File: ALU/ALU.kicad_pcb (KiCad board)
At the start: 4 copper layers, 100 x 100 mm, 78 parts, among them IC1 SN74AHCT16245DGGR, J1 Conn_01x06_Pin, J2 Conn_02x15_Odd_Even, J3 Conn_02x15_Odd_Even, J4 Conn_02x15_Odd_Even, J5 Conn_01x01_Pin, J6 Conn_01x01_Pin, J7 Conn_01x01_Pin, J8 Conn_01x01_Pin, J9 Conn_01x02, U1 74AHC1G08, U10 74HCT21, U11 74AHC1G32DBVR, U12 74AHCT1G02DBVR, U13 74AHCT1G08DBVR, U14 74AHCT1G08DBVR, U15 74AHC1G32DBVR, U16 74AHC1G32DBVR, U17 74AHC1G08, U18 SN74AHCT16374DGGR, U19 74AHCT1G08DBVR, U2 SN74AHCT16374DGGR, U20 74AHCT1G02DBVR, U21 74AHCT1G02DBVR, U3 74AHC1G04DBVR, U4 74LS181, U5 74LS181, U6 74AHCT1G08DBVR, U7 74HCT11, U8 74LS181, U9 74LS181

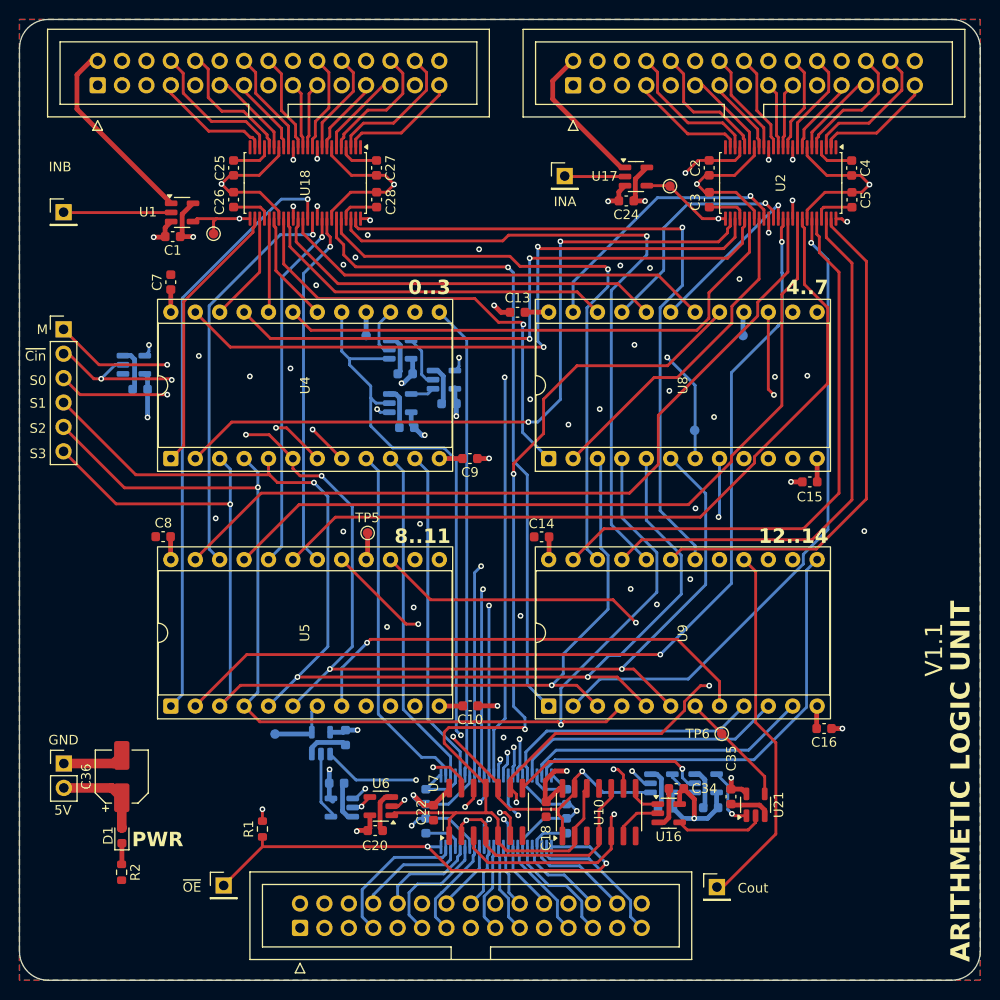
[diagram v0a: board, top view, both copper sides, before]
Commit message: Fixed register data flow direction and added mounitng holes to ALU
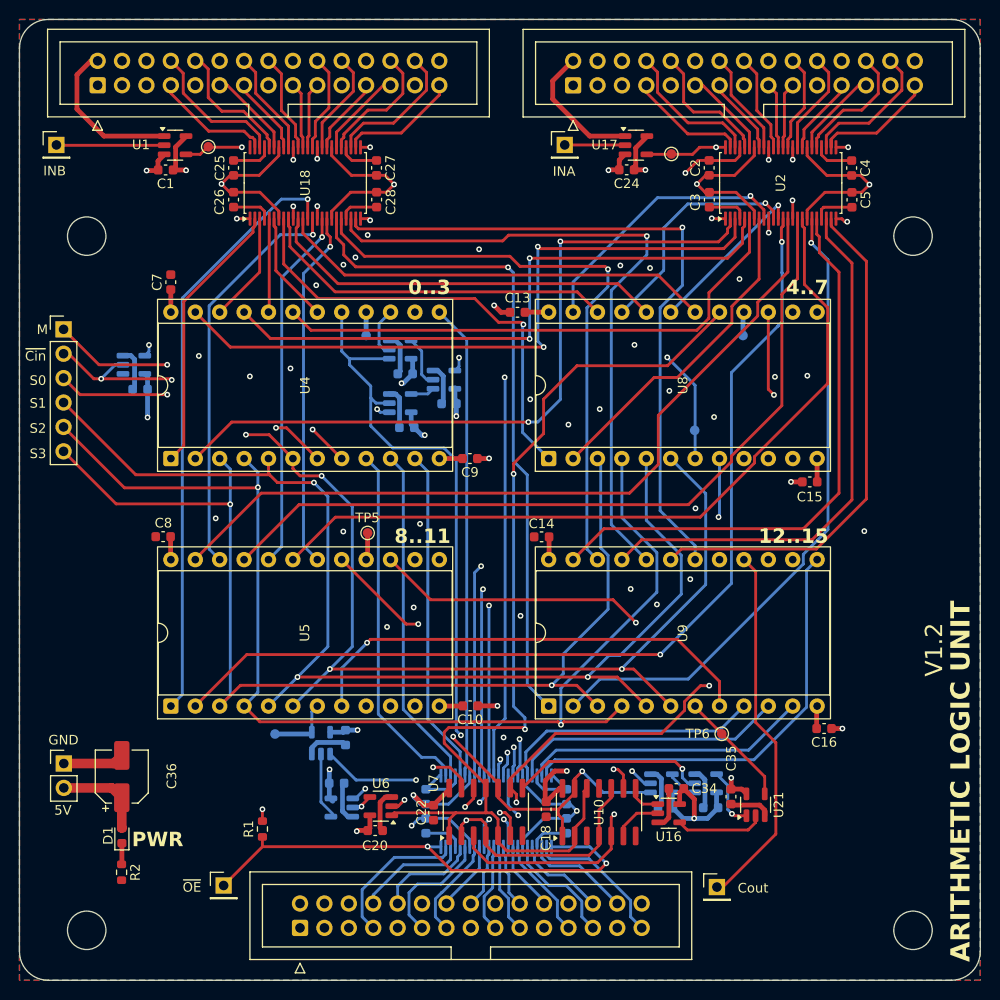
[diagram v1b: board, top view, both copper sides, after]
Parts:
- added H1: MountingHole, MountingHole:MountingHole_4mm, F.Cu at (141.0, 36.5)
- added H2: MountingHole, MountingHole:MountingHole_4mm, F.Cu at (227.0, 36.5)
- added H3: MountingHole, MountingHole:MountingHole_4mm, F.Cu at (141.0, 108.8)
- added H4: MountingHole, MountingHole:MountingHole_4mm, F.Cu at (227.0, 108.8)
- moved TP2 9.07 mm to (153.7, 27.2)
- moved J6 7.04 mm to (137.8, 27.1)
- moved U1 7.04 mm to (150.2, 27.1)
- moved C1 6.97 mm to (149.2, 29.7)
- moved TP1 3.35 mm to (201.8, 28.0)
- moved U17 3.26 mm to (198.2, 27.1)
- moved J5 3.24 mm to (190.8, 27.1)
- moved C24 3.24 mm to (197.2, 29.6)
- turned U18 to 90 degrees
- turned U2 to 90 degrees
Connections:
- U18 pad 11: /INB/DIN9 -> /INB/DOUT6
- U18 pad 12: /INB/DIN8 -> /INB/DOUT7
- U18 pad 13: /INB/DIN7 -> /INB/DOUT8
- U18 pad 14: /INB/DIN6 -> /INB/DOUT9
- U18 pad 16: /INB/DIN5 -> /INB/DOUT10
- U18 pad 17: /INB/DIN4 -> /INB/DOUT11
- U18 pad 19: /INB/DIN3 -> /INB/DOUT12
- U18 pad 2: /INB/DIN15 -> /INB/DOUT0
- U18 pad 20: /INB/DIN2 -> /INB/DOUT13
- U18 pad 22: /INB/DIN1 -> /INB/DOUT14
- U18 pad 23: /INB/DIN0 -> /INB/DOUT15
- U18 pad 26: /INB/DOUT0 -> /INB/DIN15
- U18 pad 27: /INB/DOUT1 -> /INB/DIN14
- U18 pad 29: /INB/DOUT2 -> /INB/DIN13
- U18 pad 3: /INB/DIN14 -> /INB/DOUT1
- U18 pad 30: /INB/DOUT3 -> /INB/DIN12
- U18 pad 32: /INB/DOUT4 -> /INB/DIN11
- U18 pad 33: /INB/DOUT5 -> /INB/DIN10
- U18 pad 35: /INB/DOUT6 -> /INB/DIN9
- U18 pad 36: /INB/DOUT7 -> /INB/DIN8
- U18 pad 37: /INB/DOUT8 -> /INB/DIN7
- U18 pad 38: /INB/DOUT9 -> /INB/DIN6
- U18 pad 40: /INB/DOUT10 -> /INB/DIN5
- U18 pad 41: /INB/DOUT11 -> /INB/DIN4
- U18 pad 43: /INB/DOUT12 -> /INB/DIN3
- U18 pad 44: /INB/DOUT13 -> /INB/DIN2
- U18 pad 46: /INB/DOUT14 -> /INB/DIN1
- U18 pad 47: /INB/DOUT15 -> /INB/DIN0
- U18 pad 5: /INB/DIN13 -> /INB/DOUT2
- U18 pad 6: /INB/DIN12 -> /INB/DOUT3
- U18 pad 8: /INB/DIN11 -> /INB/DOUT4
- U18 pad 9: /INB/DIN10 -> /INB/DOUT5
- U2 pad 11: /INA/DIN9 -> /INA/DOUT6
- U2 pad 12: /INA/DIN8 -> /INA/DOUT7
- U2 pad 13: /INA/DIN7 -> /INA/DOUT8
- U2 pad 14: /INA/DIN6 -> /INA/DOUT9
- U2 pad 16: /INA/DIN5 -> /INA/DOUT10
- U2 pad 17: /INA/DIN4 -> /INA/DOUT11
- U2 pad 19: /INA/DIN3 -> /INA/DOUT12
- U2 pad 2: /INA/DIN15 -> /INA/DOUT0
- U2 pad 20: /INA/DIN2 -> /INA/DOUT13
- U2 pad 22: /INA/DIN1 -> /INA/DOUT14
- U2 pad 23: /INA/DIN0 -> /INA/DOUT15
- U2 pad 26: /INA/DOUT0 -> /INA/DIN15
- U2 pad 27: /INA/DOUT1 -> /INA/DIN14
- U2 pad 29: /INA/DOUT2 -> /INA/DIN13
- U2 pad 3: /INA/DIN14 -> /INA/DOUT1
- U2 pad 30: /INA/DOUT3 -> /INA/DIN12
- U2 pad 32: /INA/DOUT4 -> /INA/DIN11
- U2 pad 33: /INA/DOUT5 -> /INA/DIN10
- U2 pad 35: /INA/DOUT6 -> /INA/DIN9
- U2 pad 36: /INA/DOUT7 -> /INA/DIN8
- U2 pad 37: /INA/DOUT8 -> /INA/DIN7
- U2 pad 38: /INA/DOUT9 -> /INA/DIN6
- U2 pad 40: /INA/DOUT10 -> /INA/DIN5
- U2 pad 41: /INA/DOUT11 -> /INA/DIN4
- U2 pad 43: /INA/DOUT12 -> /INA/DIN3
- U2 pad 44: /INA/DOUT13 -> /INA/DIN2
- U2 pad 46: /INA/DOUT14 -> /INA/DIN1
- U2 pad 47: /INA/DOUT15 -> /INA/DIN0
- U2 pad 5: /INA/DIN13 -> /INA/DOUT2
- U2 pad 6: /INA/DIN12 -> /INA/DOUT3
- U2 pad 8: /INA/DIN11 -> /INA/DOUT4
- U2 pad 9: /INA/DIN10 -> /INA/DOUT5
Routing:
- net GND: track 154.8 -> 160.1 mm, vias 47 -> 51
- net /bus_connector2/CLK: track 20.2 -> 16.6 mm
- net Net-(U18-1CLK): track 22.4 -> 20.5 mm
- net /bus_connector/CLK: track 15.3 -> 14.0 mm
- net Net-(U2-1CLK): track 24.4 -> 23.5 mm
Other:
- board text added: "12..15"
- board text added: "V1.2"
- board text removed: "12..14"
- board text removed: "V1.1"

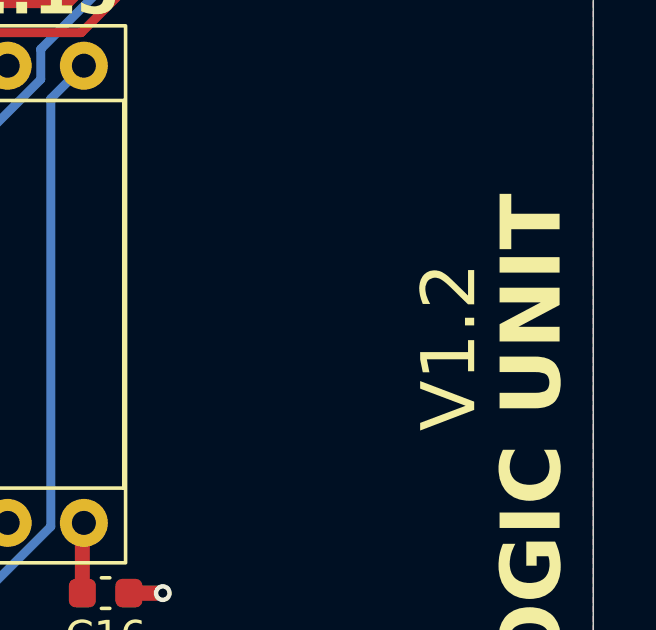
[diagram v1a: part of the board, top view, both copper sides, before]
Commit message: Refactored files, finalized reg4x16, and used lowercase v
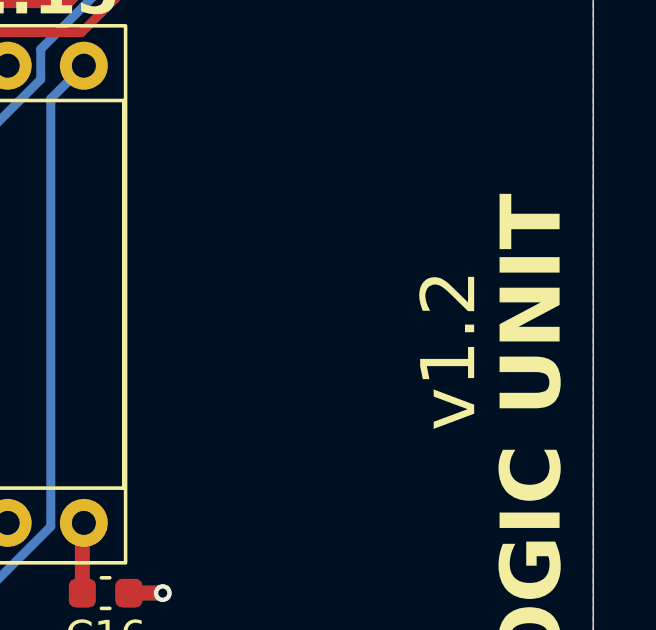
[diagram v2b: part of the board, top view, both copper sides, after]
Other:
- board text added: "v1.2"
- board text removed: "V1.2"
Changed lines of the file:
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@@
 	(paper "A4")
 	(title_block
-		(date "2025-09-03")
-		(rev "V1.2")
+		(date "2025-09-05")
+		(rev "v1.2")
 	)
 	(layers
@@
 		)
 	)
-	(gr_text "V1.2\n"
+	(gr_text "v1.2\n"
 		(at 230.25 82.4 90)
 		(layer "F.SilkS")

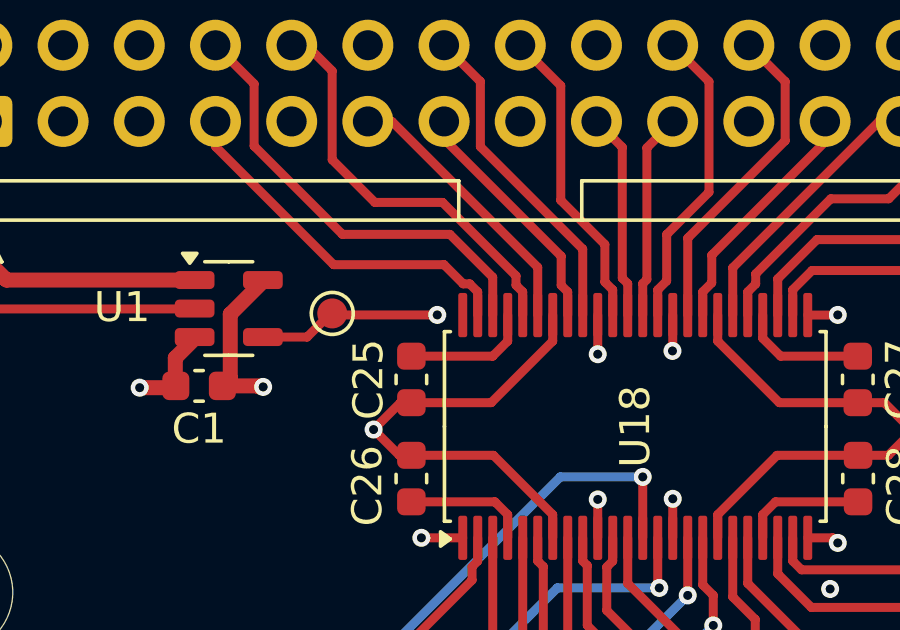
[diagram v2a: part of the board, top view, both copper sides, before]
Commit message: Memory Controller fabrication checks complete
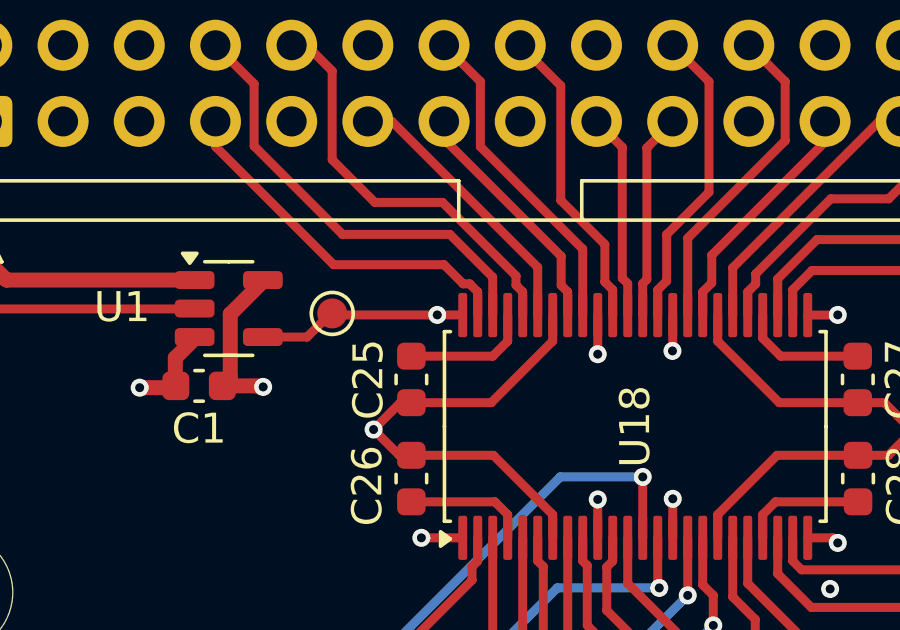
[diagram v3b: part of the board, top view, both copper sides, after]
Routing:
- net Net-(U18-1CLK): track 20.5 -> 21.3 mm
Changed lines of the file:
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@@
 		(tenting none)
 		(pcbplotparams
-			(layerselection 0x00000000_00000000_55555555_575555ff)
+			(layerselection 0x00000000_00000000_55555555_5755f5ff)
 			(plot_on_all_layers_selection 0x00000000_00000000_00000000_00000000)
 			(disableapertmacros no)
@@
 	)
 	(segment
+		(start 157.15 27.3)
+		(end 157.9941 27.3)
+		(width 0.3)
+		(layer "F.Cu")
+		(net 40)
+	)
+	(segment
 		(start 169.4991 27.305)
 		(end 170.495 27.305)
@@
 	)
 	(segment
-		(start 157.15 27.3)
-		(end 157.2 27.3)
+		(start 157.9941 27.3)
+		(end 157.9991 27.305)
 		(width 0.3)
 		(layer "F.Cu")
